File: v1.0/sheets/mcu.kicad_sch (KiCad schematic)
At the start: 16 parts, among them U4 STM32U5G7VJTx

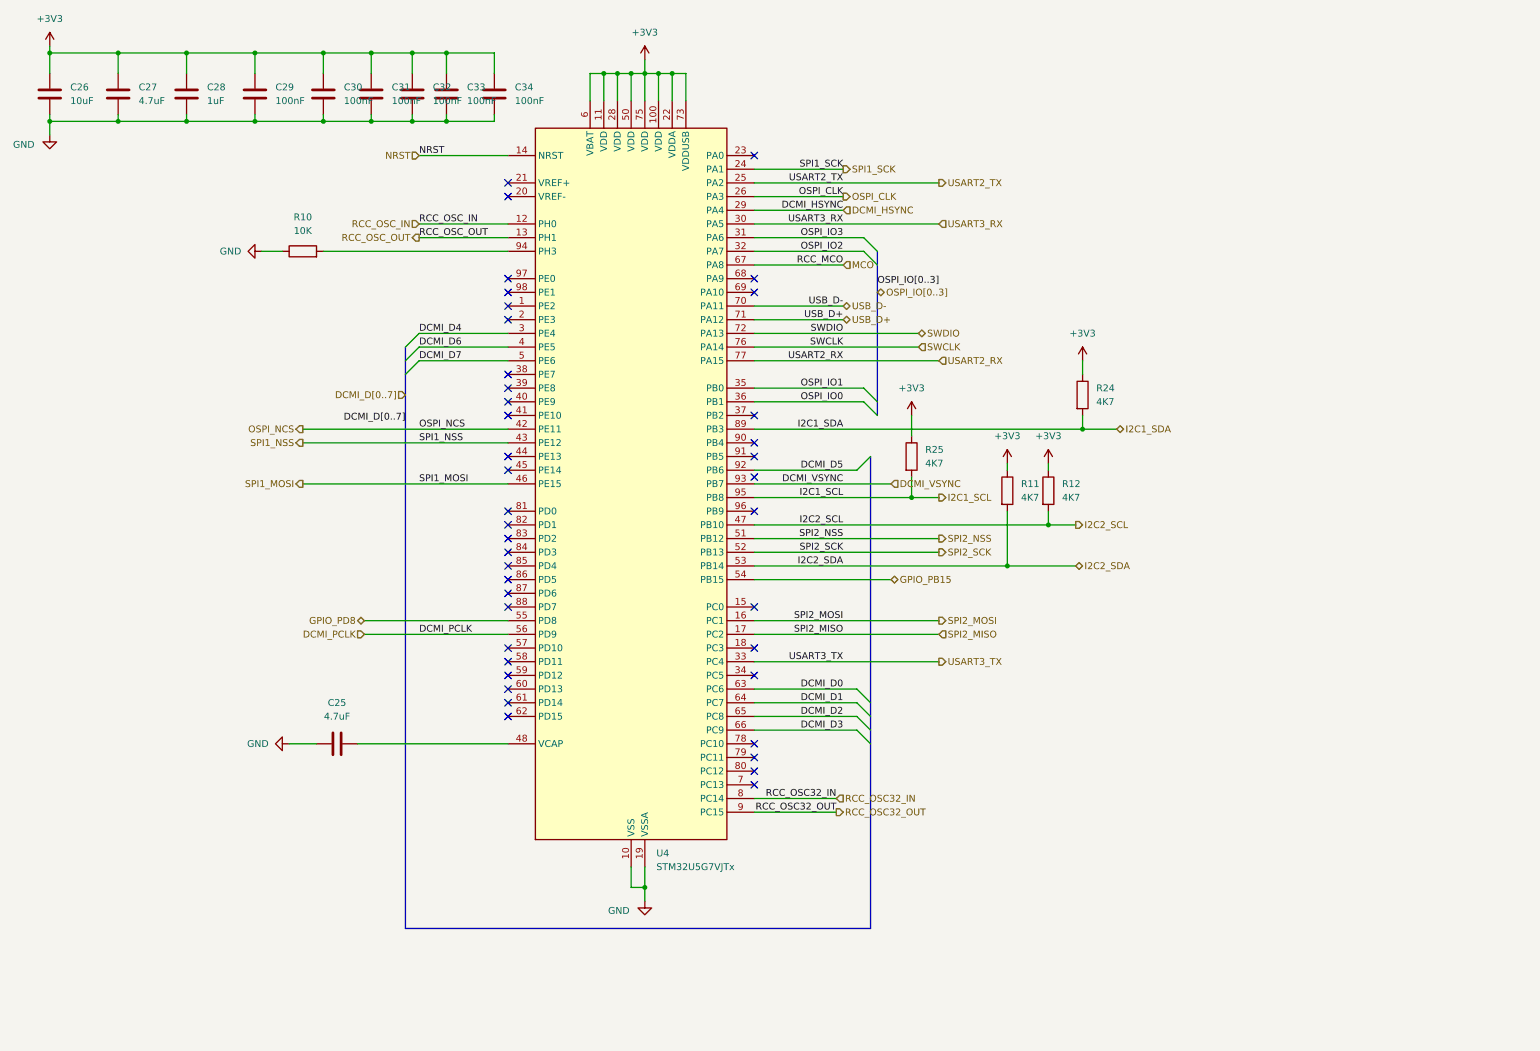
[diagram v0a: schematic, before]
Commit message: V1.0 rework to match stm32u5xxxQ
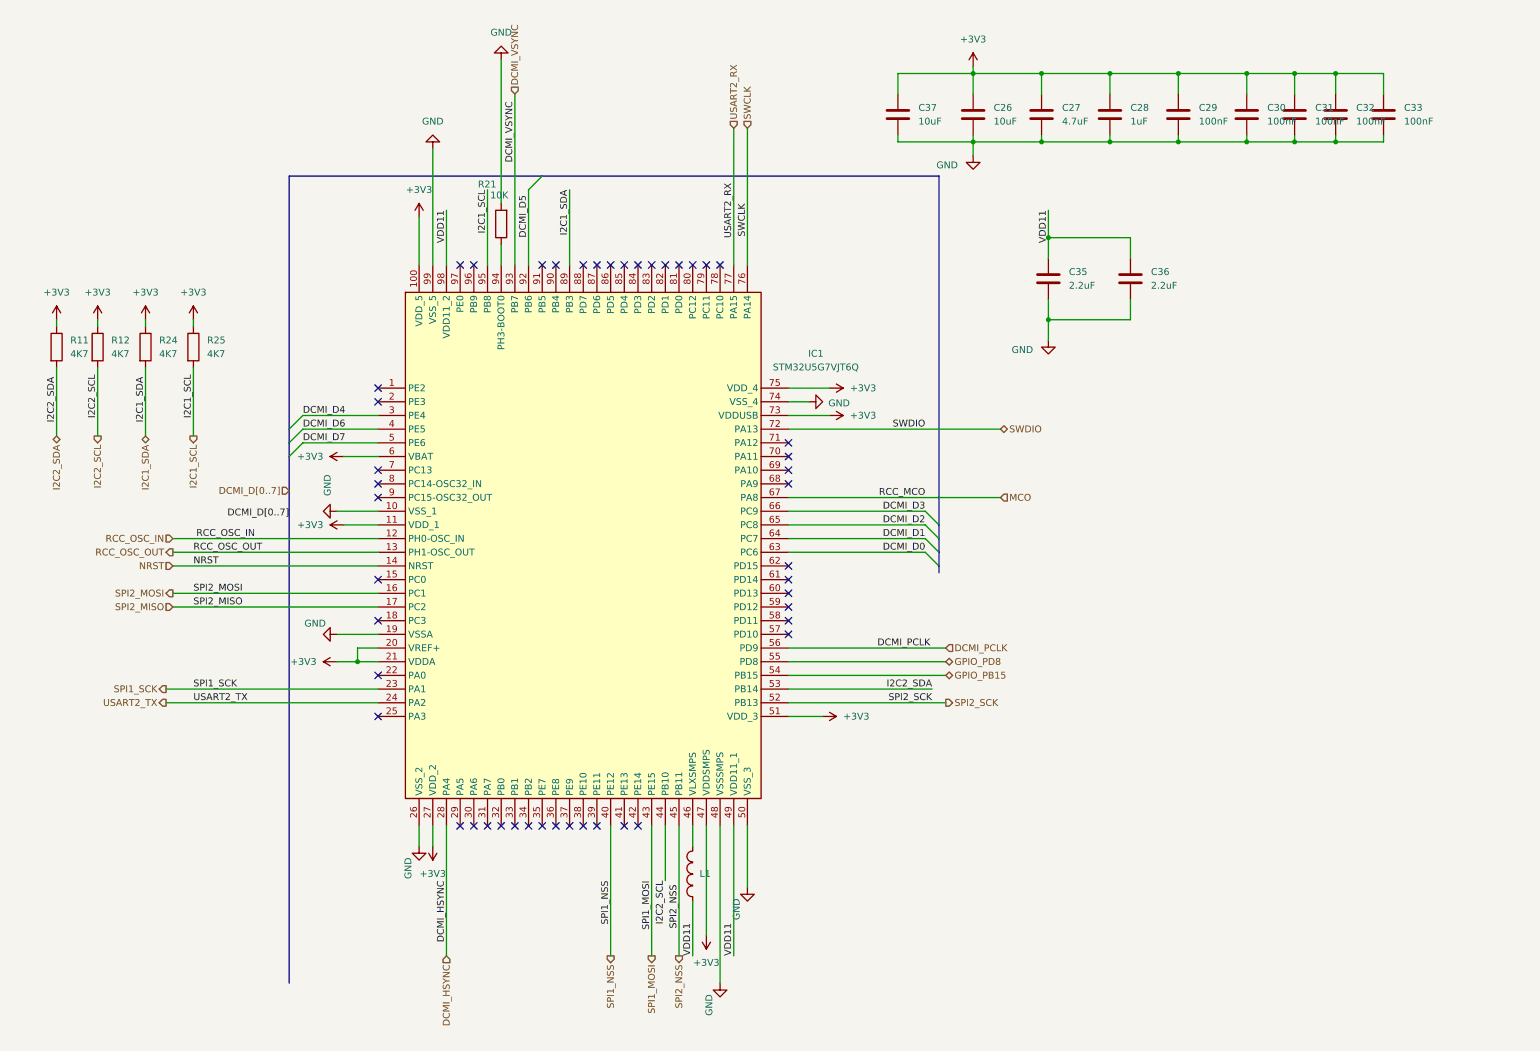
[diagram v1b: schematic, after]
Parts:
- removed C25: 4.7uF, Capacitor_SMD:C_0603_1608Metric, symbol Device:C
- removed C34: 100nF, Capacitor_SMD:C_0603_1608Metric, symbol Device:C
- removed R10: 10K, Resistor_SMD:R_0402_1005Metric, symbol Device:R
- removed U4: STM32U5G7VJTx, Package_QFP:LQFP-100_14x14mm_P0.5mm, symbol MCU_ST_STM32U5:STM32U5G7VJTx
- added C35, C36: 2.2uF, Capacitor_SMD:C_0603_1608Metric, symbol Device:C
- added C37: 10uF, Capacitor_SMD:C_0805_2012Metric, symbol Device:C
- added IC1: STM32U5G7VJT6Q, Package_QFP:LQFP-100_14x14mm_P0.5mm, symbol Grinreflex:STM32U5G7VJT6Q
- added L1: 2.2uH, Grinreflex:IND-SMD_L2.4-W1.7_NL201614, symbol Grinreflex:SWPA252012S2R2N
- added R21: 10K, Resistor_SMD:R_0402_1005Metric, symbol Device:R
- C29, C30, C32, C33: footprint Capacitor_SMD:C_0603_1608Metric -> Capacitor_SMD:C_0402_1005Metric
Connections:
- net +3V3: now also C37.2, IC1.100 (VDD_5), IC1.11 (VDD_1), IC1.20 (VREF+), IC1.21 (VDDA), IC1.27 (VDD_2), IC1.47 (VDDSMPS), IC1.51 (VDD_3), IC1.6 (VBAT), IC1.73 (VDDUSB), IC1.75 (VDD_4)
- net DCMI_D0: now also IC1.63 (PC6)
- net DCMI_D1: now also IC1.64 (PC7)
- net DCMI_D2: now also IC1.65 (PC8)
- net DCMI_D3: now also IC1.66 (PC9)
- net DCMI_D4: now also IC1.3 (PE4)
- net DCMI_D5: now also IC1.92 (PB6)
- net DCMI_D6: now also IC1.4 (PE5)
- net DCMI_D7: now also IC1.5 (PE6)
- net DCMI_HSYNC: now also IC1.28 (PA4)
- net DCMI_PCLK: now also IC1.56 (PD9)
- net DCMI_VSYNC: now also IC1.93 (PB7)
- net GND: now also C35.1, C36.1, C37.1, IC1.10 (VSS_1), IC1.19 (VSSA), IC1.26 (VSS_2), IC1.48 (VSSSMPS), IC1.50 (VSS_3), IC1.74 (VSS_4), IC1.99 (VSS_5), R21.2
- net GPIO_PB15: now also IC1.54 (PB15)
- net GPIO_PD8: now also IC1.55 (PD8)
- net I2C1_SCL: now also IC1.95 (PB8)
- net I2C1_SDA: now also IC1.89 (PB3)
- net I2C2_SCL: now also IC1.44 (PB10)
- net I2C2_SDA: now also IC1.53 (PB14)
- net MCO: now also IC1.67 (PA8)
- net NRST: now also IC1.14 (NRST)
- net RCC_OSC_IN: now also IC1.12 (PH0-OSC_IN)
- net RCC_OSC_OUT: now also IC1.13 (PH1-OSC_OUT)
- net SPI1_MOSI: now also IC1.43 (PE15)
- net SPI1_NSS: now also IC1.40 (PE12)
- net SPI1_SCK: now also IC1.23 (PA1)
- net SPI2_MISO: now also IC1.17 (PC2)
- net SPI2_MOSI: now also IC1.16 (PC1)
- net SPI2_NSS: now also IC1.45 (PB11)
- net SPI2_SCK: now also IC1.52 (PB13)
- net SWCLK: now also IC1.76 (PA14)
- net SWDIO: now also IC1.72 (PA13)
- net USART2_RX: now also IC1.77 (PA15)
- net USART2_TX: now also IC1.24 (PA2)
- new net: IC1.94 (PH3-BOOT0), R21.1
- new net: IC1.46 (VLXSMPS), L1.2
- new net VDD11: C35.2, C36.2, IC1.49 (VDD11_1), IC1.98 (VDD11_2), L1.1
- no-connect marks 41 -> 47
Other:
- moved on the sheet: C26, C27, C28, C29, C30, C31, C32, C33, R11, R12, R24, R25

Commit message: Revision V2.0 finalized
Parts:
- added C34, C38, C39, C40, C41: 100nF, Capacitor_SMD:C_0402_1005Metric, symbol Device:C
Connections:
- net +3V3: now also C34.2, C38.2, C39.2, C40.2, C41.2
- net GND: now also C34.1, C38.1, C39.1, C40.1, C41.1
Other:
- moved on the sheet: C26, C27, C28, C29, C30, C31, C32, C33, C37
